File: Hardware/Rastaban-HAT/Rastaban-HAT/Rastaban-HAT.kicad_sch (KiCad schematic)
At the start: 60 parts, among them IC1 P82B96TD,118, J1 Screw_Terminal_01x04, J10 GPIO, J11 Conn_01x06_Male, J2 Screw_Terminal_01x04, J3 Screw_Terminal_01x04, J4 Screw_Terminal_01x02, J5 Jack-DC 12V+, J6 SM04B-SRSS-TB(LF)(SN), J7 Screw_Terminal_01x02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

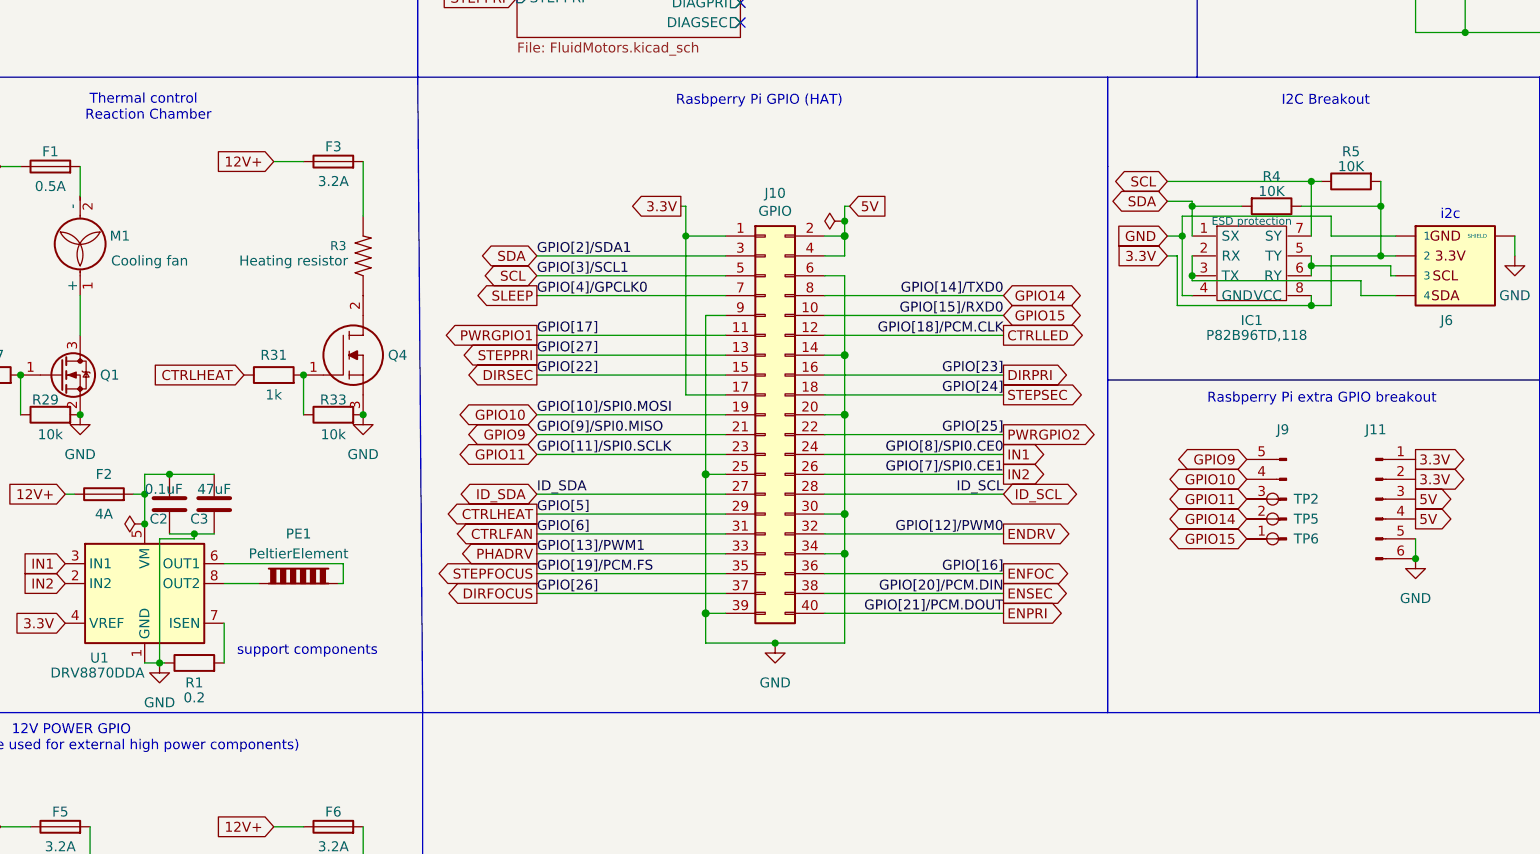
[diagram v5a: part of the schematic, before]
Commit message: new i2c protection circuit
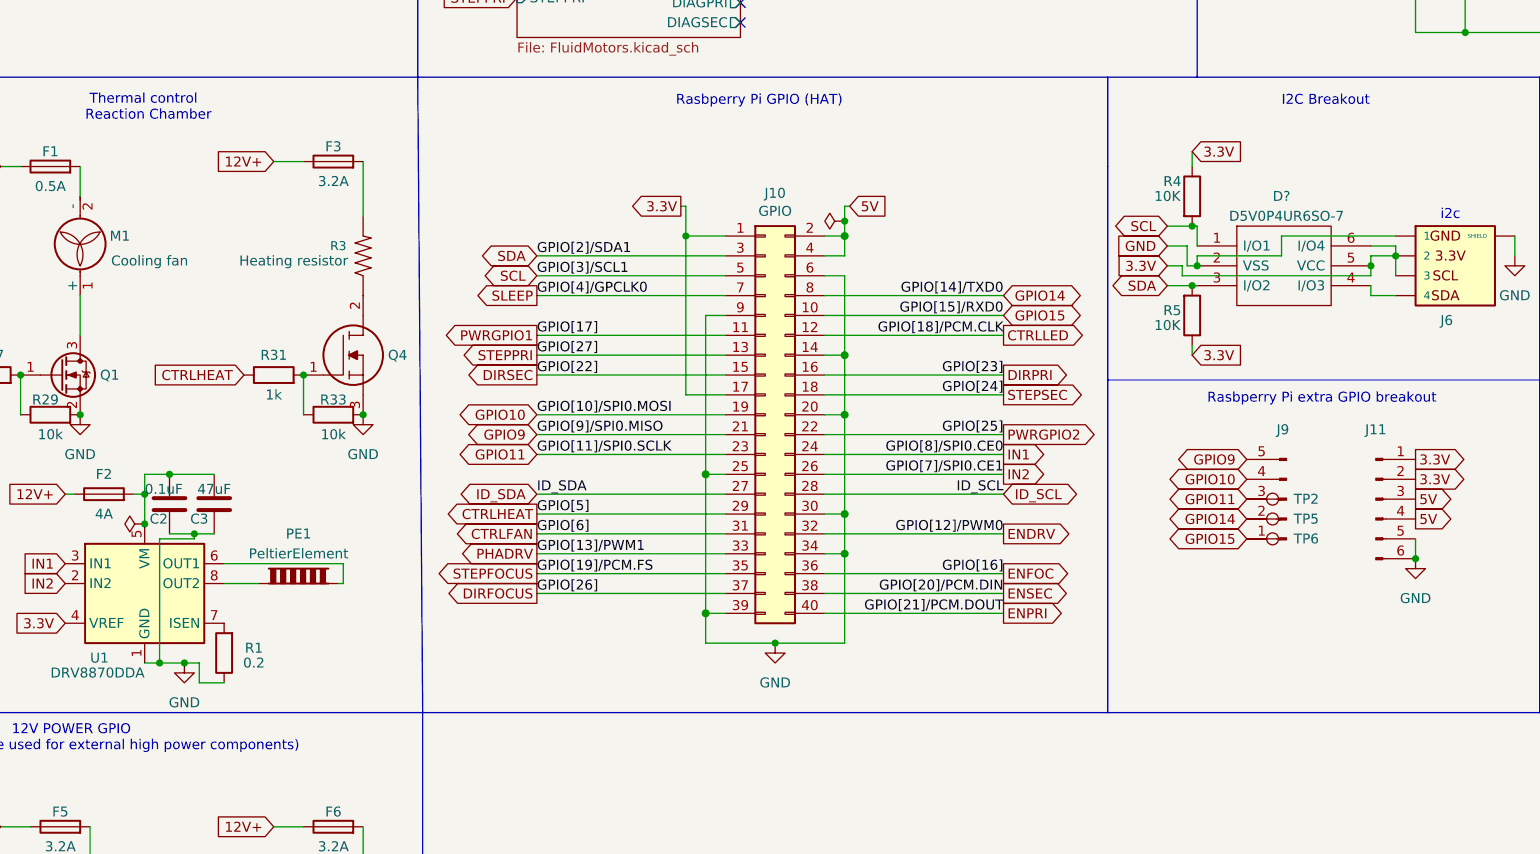
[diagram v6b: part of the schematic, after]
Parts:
- removed IC1: P82B96TD,118, SmacSYs:SOIC127P600X175-8N, symbol SamacSys_Parts:P82B96TD,118
- added D?: D5V0P4UR6SO-7, SOT95P285X140-6N, symbol SamacSys_Parts:D5V0P4UR6SO-7
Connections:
- net 3.3V: now also J6.3, R5.1, D?.5 (VCC), D?.6 (I/O4); no longer R5.2
- net GND: now also D?.2 (VSS)
- net SCL: now also R4.2, D?.1 (I/O1); no longer R5.1
- net SDA: now also R5.2, D?.3 (I/O2); no longer R4.2
- net at J6.4: now also D?.4 (I/O3)
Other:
- note removed: "support components"
- moved on the sheet: R1, R4, R5

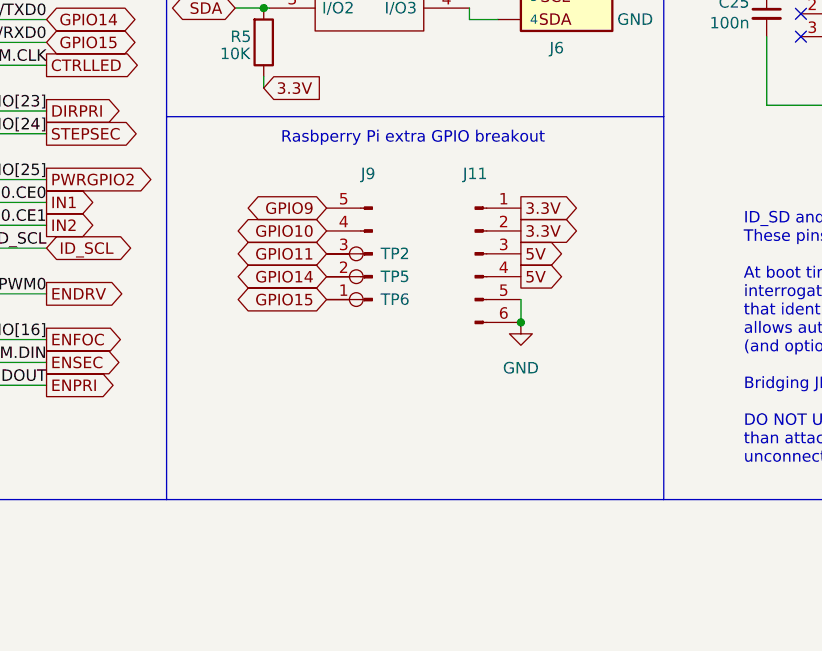
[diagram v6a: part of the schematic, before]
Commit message: added ESD protection to some GPIO breakout pins
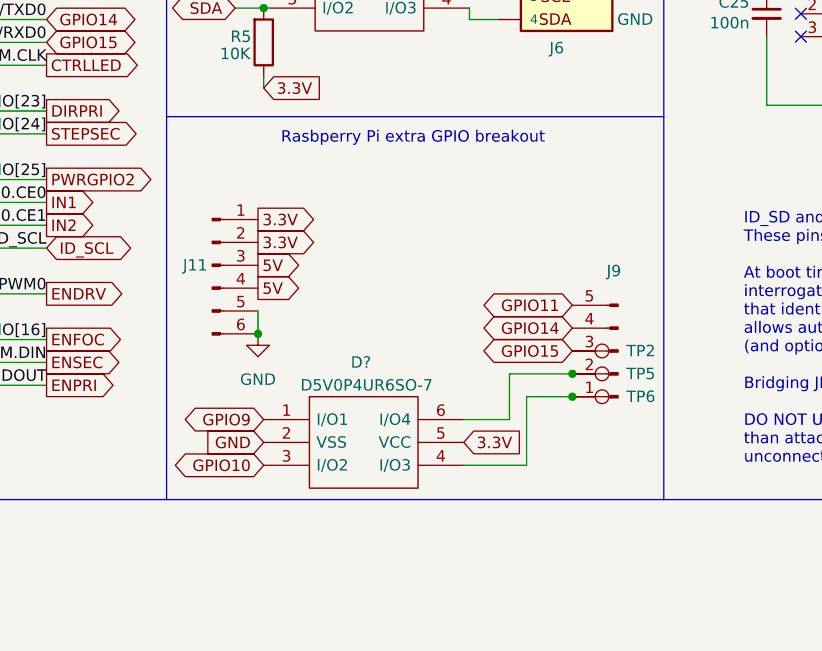
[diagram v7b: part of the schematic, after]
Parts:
- added D?: D5V0P4UR6SO-7, SOT95P285X140-6N, symbol SamacSys_Parts:D5V0P4UR6SO-7
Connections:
- net 3.3V: now also D?.5 (VCC)
- net GND: now also D?.2 (VSS)
- net GPIO10: now also D?.3 (I/O2); no longer J9.4 (Pin_4)
- net GPIO11: now also J9.5 (Pin_5); no longer J9.3 (Pin_3), TP2.1
- net GPIO14: now also J9.4 (Pin_4); no longer J9.2 (Pin_2), TP5.1
- net GPIO15: now also J9.3 (Pin_3), TP2.1; no longer J9.1 (Pin_1), TP6.1
- net GPIO9: now also D?.1 (I/O1); no longer J9.5 (Pin_5)
- new net: D?.4 (I/O3), J9.1 (Pin_1), TP6.1
- new net: D?.6 (I/O4), J9.2 (Pin_2), TP5.1
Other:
- moved on the sheet: J11, J9, TP2, TP5, TP6

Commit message: Added new connectors for stepper motors Phoenix PTSM
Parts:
- removed J1, J2, J3: Screw_Terminal_01x04, Connector_JST:JST_XH_B4B-XH-A_1x04_P2.50mm_Vertical, symbol Connector:Screw_Terminal_01x04
- added J? (x3): 1778780, 1778780, symbol SamacSys_Parts:1778780
- gave numbers to parts that had none: 2
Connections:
- net FluidMotors/OA1PRI: now also J?.4
- net FluidMotors/OA1SEC: now also J?.4
- net FluidMotors/OA2PRI: now also J?.3
- net FluidMotors/OA2SEC: now also J?.3
- net FluidMotors/OB1PRI: now also J?.2
- net FluidMotors/OB1SEC: now also J?.2
- net FluidMotors/OB2PRI: now also J?.1
- net FluidMotors/OB2SEC: now also J?.1
- net FocusMotors/OA1FOCUS: now also J?.4
- net FocusMotors/OA2FOCUS: now also J?.3
- net FocusMotors/OB1FOCUS: now also J?.2
- net FocusMotors/OB2FOCUS: now also J?.1
- net FocusMotors/out1: now also J4.2 (Pin_2); no longer J4.1 (Pin_1)
- net FocusMotors/out2: now also J4.1 (Pin_1); no longer J4.2 (Pin_2)
- net GND: now also J?.5, J?.5, J?.5, J?.6, J?.6, J?.6
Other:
- moved on the sheet: J4
